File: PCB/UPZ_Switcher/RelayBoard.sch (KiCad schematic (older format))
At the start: 32 parts, among them K1 TQ2SA-5V-Z, K10 TQ2SA-5V-Z, K11 TQ2SA-5V-Z, K12 TQ2SA-5V-Z, K13 TQ2SA-5V-Z, K14 TQ2SA-5V-Z, K15 TQ2SA-5V-Z, K16 TQ2SA-5V-Z, K17 TQ2SA-5V-Z, K18 TQ2SA-5V-Z, K2 TQ2SA-5V-Z, K3 TQ2SA-5V-Z, K4 TQ2SA-5V-Z, K5 TQ2SA-5V-Z, K6 TQ2SA-5V-Z, K7 TQ2SA-5V-Z, K8 TQ2SA-5V-Z, K9 TQ2SA-5V-Z

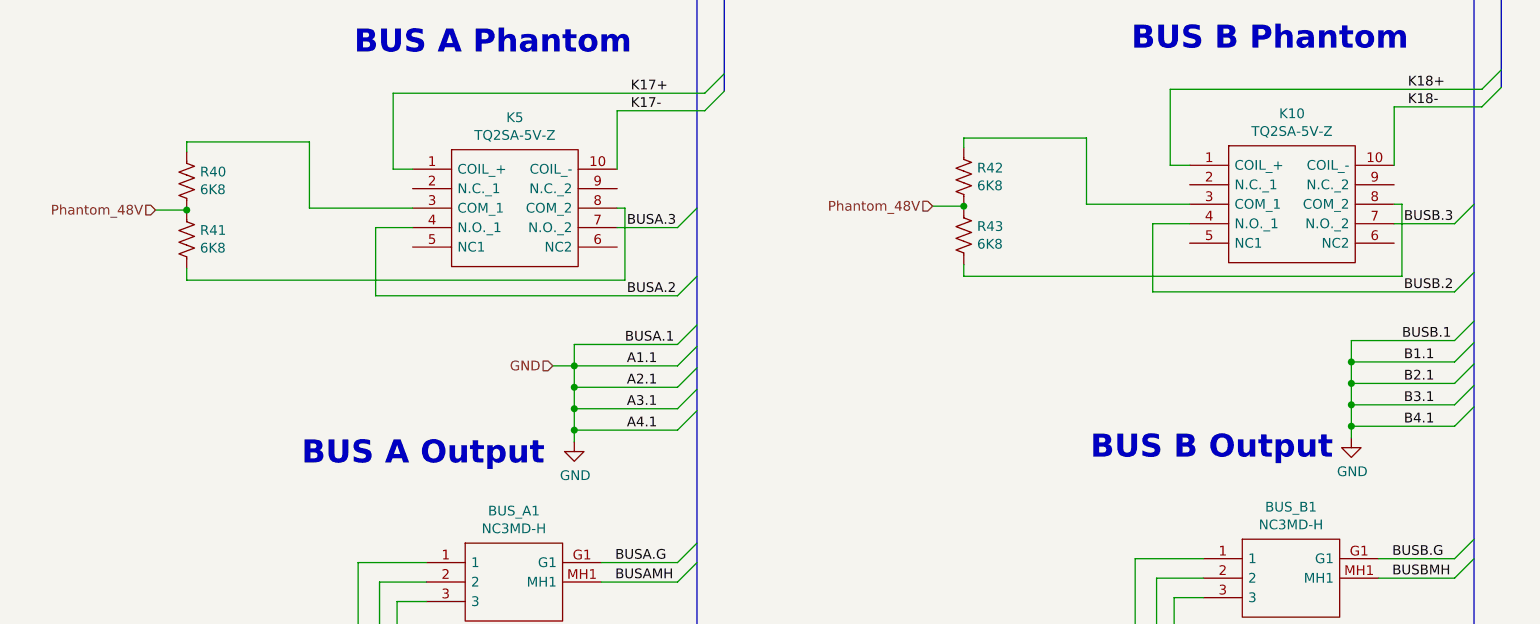
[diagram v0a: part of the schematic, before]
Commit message: Updated schematic, PSU added + draft program
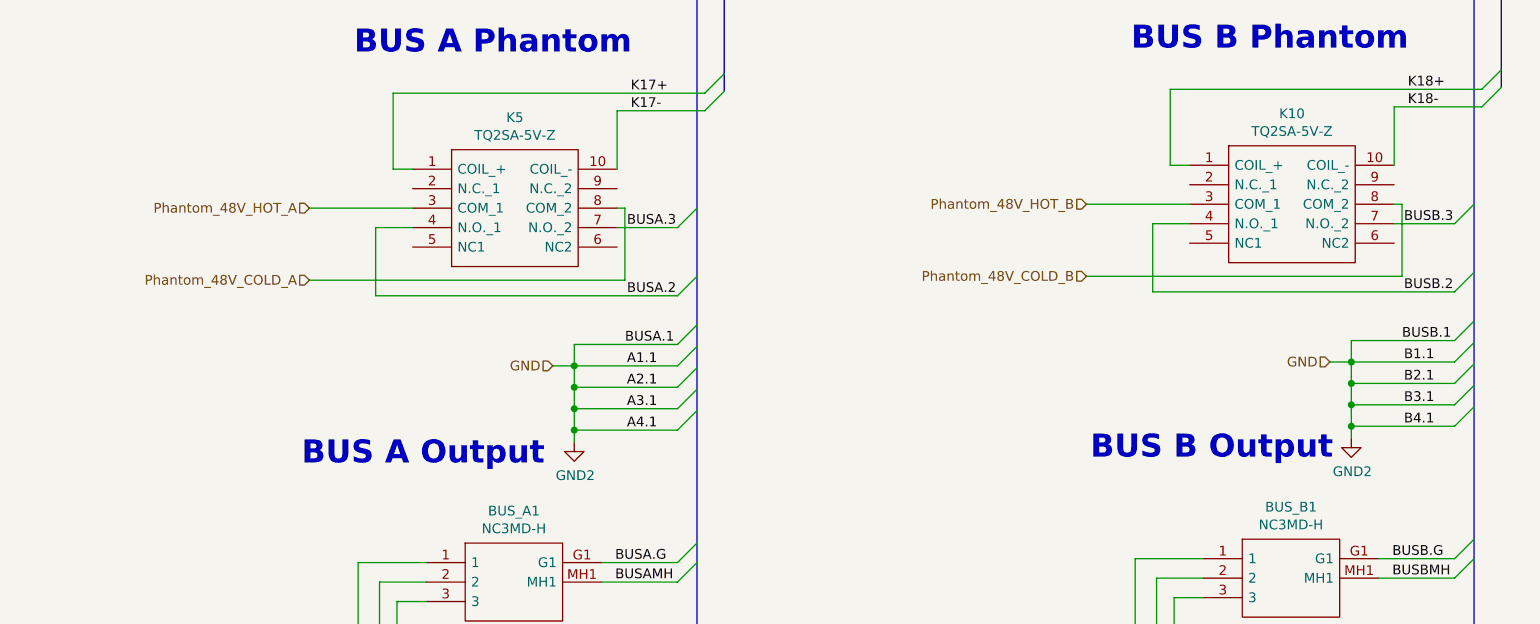
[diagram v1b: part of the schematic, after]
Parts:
- removed R40, R41, R42, R43: 6K8, Resistor_SMD:R_1206_3216Metric, symbol Device:R_US
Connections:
- net Phantom_48V_HOT_A: now reaches K5.3 (COM_1)
- net Phantom_48V_COLD_A: now reaches K5.8 (COM_2)
- net Phantom_48V_HOT_B: now reaches K10.3 (COM_1)
- net Phantom_48V_COLD_B: now reaches K10.8 (COM_2)
- net GND renamed GND2
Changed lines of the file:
@@
 $Descr A3 16535 11693
 encoding utf-8
-Sheet 5 6
+Sheet 5 5
 Title "Relay Board"
 Date "2021-02-27"
@@
 Text Label 3710 5690 0    50   ~ 0
 K17-
-Text HLabel 1270 6200 0    50   Input ~ 0
-Phantom_48V
+Text HLabel 2060 6190 0    50   Input ~ 0
+Phantom_48V_HOT_A
 Wire Wire Line
 	3640 6190 3680 6190
 Wire Wire Line
-	1270 6200 1430 6200
-Wire Wire Line
 	2590 6290 2400 6290
 Wire Wire Line
@@
 Wire Wire Line
 	2400 6640 3950 6640
-$Comp
-L Device:R_US R41
-U 1 1 6067E759
-P 1430 6350
-AR Path="/62E5E978/6067E759" Ref="R41"  Part="1"
-AR Path="/62E8A761/6067E759" Ref="R?"  Part="1"
-F 0 "R41" H 1498 6396 50  0000 L CNN
-F 1 "6K8" H 1498 6305 50  0000 L CNN
-F 2 "Resistor_SMD:R_1206_3216Metric" V 1470 6340 50  0001 C CNN
-F 3 "~" H 1430 6350 50  0001 C CNN
-	1    1430 6350
-	1    0    0    -1
-$EndComp
-$Comp
-L Device:R_US R40
-U 1 1 6067F0FC
-P 1430 6050
-AR Path="/62E5E978/6067F0FC" Ref="R40"  Part="1"
-AR Path="/62E8A761/6067F0FC" Ref="R?"  Part="1"
-F 0 "R40" H 1498 6096 50  0000 L CNN
-F 1 "6K8" H 1498 6005 50  0000 L CNN
-F 2 "Resistor_SMD:R_1206_3216Metric" V 1470 6040 50  0001 C CNN
-F 3 "~" H 1430 6050 50  0001 C CNN
-	1    1430 6050
-	1    0    0    -1
-$EndComp
-Connection ~ 1430 6200
-Wire Wire Line
-	2060 5850 1430 5850
 Wire Wire Line
 	2060 6190 2590 6190
-Wire Wire Line
-	1430 6500 1430 6560
-Wire Wire Line
-	2060 5850 2060 6190
-Wire Wire Line
-	1430 5900 1430 5850
 Text Label 3690 6640 0    50   ~ 0
 BUSA.2
-Wire Wire Line
-	1430 6560 3680 6560
 Wire Wire Line
 	3680 6190 3680 6560
@@
 Text Label 7700 5670 0    50   ~ 0
 K18-
-Text HLabel 5260 6180 0    50   Input ~ 0
-Phantom_48V
 Wire Wire Line
 	7630 6170 7670 6170
 Wire Wire Line
-	5260 6180 5420 6180
-Wire Wire Line
 	6580 6270 6390 6270
 Wire Wire Line
@@
 Wire Wire Line
 	6390 6620 7940 6620
-$Comp
-L Device:R_US R43
-U 1 1 60721959
-P 5420 6330
-AR Path="/62E5E978/60721959" Ref="R43"  Part="1"
-AR Path="/62E8A761/60721959" Ref="R?"  Part="1"
-F 0 "R43" H 5488 6376 50  0000 L CNN
-F 1 "6K8" H 5488 6285 50  0000 L CNN
-F 2 "Resistor_SMD:R_1206_3216Metric" V 5460 6320 50  0001 C CNN
-F 3 "~" H 5420 6330 50  0001 C CNN
-	1    5420 6330
-	1    0    0    -1
-$EndComp
-$Comp
-L Device:R_US R42
-U 1 1 60721963
-P 5420 6030
-AR Path="/62E5E978/60721963" Ref="R42"  Part="1"
-AR Path="/62E8A761/60721963" Ref="R?"  Part="1"
-F 0 "R42" H 5488 6076 50  0000 L CNN
-F 1 "6K8" H 5488 5985 50  0000 L CNN
-F 2 "Resistor_SMD:R_1206_3216Metric" V 5460 6020 50  0001 C CNN
-F 3 "~" H 5420 6030 50  0001 C CNN
-	1    5420 6030
-	1    0    0    -1
-$EndComp
-Connection ~ 5420 6180
-Wire Wire Line
-	6050 5830 5420 5830
 Wire Wire Line
 	6050 6170 6580 6170
-Wire Wire Line
-	5420 6480 5420 6540
-Wire Wire Line
-	6050 5830 6050 6170
-Wire Wire Line
-	5420 5880 5420 5830
 Text Label 7680 6620 0    50   ~ 0
 BUSB.2
-Wire Wire Line
-	5420 6540 7670 6540
 Wire Wire Line
 	7670 6170 7670 6540
@@
 BUSB.1
 $Comp
-L power:GND #PWR0121
+L power:GND2 #PWR0121
 U 1 1 609411A2
 P 7410 7370
@@
 AR Path="/62E8A761/609411A2" Ref="#PWR?"  Part="1"
 F 0 "#PWR0121" H 7410 7120 50  0001 C CNN
-F 1 "GND" H 7415 7197 50  0000 C CNN
+F 1 "GND2" H 7415 7197 50  0000 C CNN
 F 2 "" H 7410 7370 50  0001 C CNN
 F 3 "" H 7410 7370 50  0001 C CNN
@@
 	4050 6790 3950 6890
 $Comp
-L power:GND #PWR0122
+L power:GND2 #PWR0122
 U 1 1 6087E8BE
 P 3420 7390
@@
 AR Path="/62E8A761/6087E8BE" Ref="#PWR?"  Part="1"
 F 0 "#PWR0122" H 3420 7140 50  0001 C CNN
-F 1 "GND" H 3425 7217 50  0000 C CNN
+F 1 "GND2" H 3425 7217 50  0000 C CNN
 F 2 "" H 3420 7390 50  0001 C CNN
 F 3 "" H 3420 7390 50  0001 C CNN
@@
 Wire Wire Line
 	3310 7000 3420 7000
+Text HLabel 2060 6560 0    50   Input ~ 0
+Phantom_48V_COLD_A
+Text HLabel 6050 6170 0    50   Input ~ 0
+Phantom_48V_HOT_B
+Text HLabel 6050 6540 0    50   Input ~ 0
+Phantom_48V_COLD_B
+Wire Wire Line
+	3680 6560 2060 6560
+Wire Wire Line
+	7670 6540 6050 6540
+Text HLabel 7300 6980 0    50   Input ~ 0
+GND
+Wire Wire Line
+	7300 6980 7410 6980
 Wire Bus Line
 	15960 3170 15960 3440
